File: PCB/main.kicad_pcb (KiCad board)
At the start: 2 copper layers, 112.9 x 63.7 mm, 104 parts, among them K1 HK19F-DCxxV-SHC, Q10 BC817, Q11 BC817, Q12 TPCA8120,L1Q, Q13 BC817, Q14 BC817, Q15 BC817, Q16 TPCA8120,L1Q, Q17 BC817, Q18 TPCA8120,L1Q, Q19 BC817, Q2 BC817, Q3 TPCA8120,L1Q, Q4 BC817, Q5 TPCA8120,L1Q, Q6 TPCA8120,L1Q, Q7 TPCA8120,L1Q, Q8 BC817, Q9 BC817, SW1 config, U1 ESP32-S2-DevKitM, U2 L7805

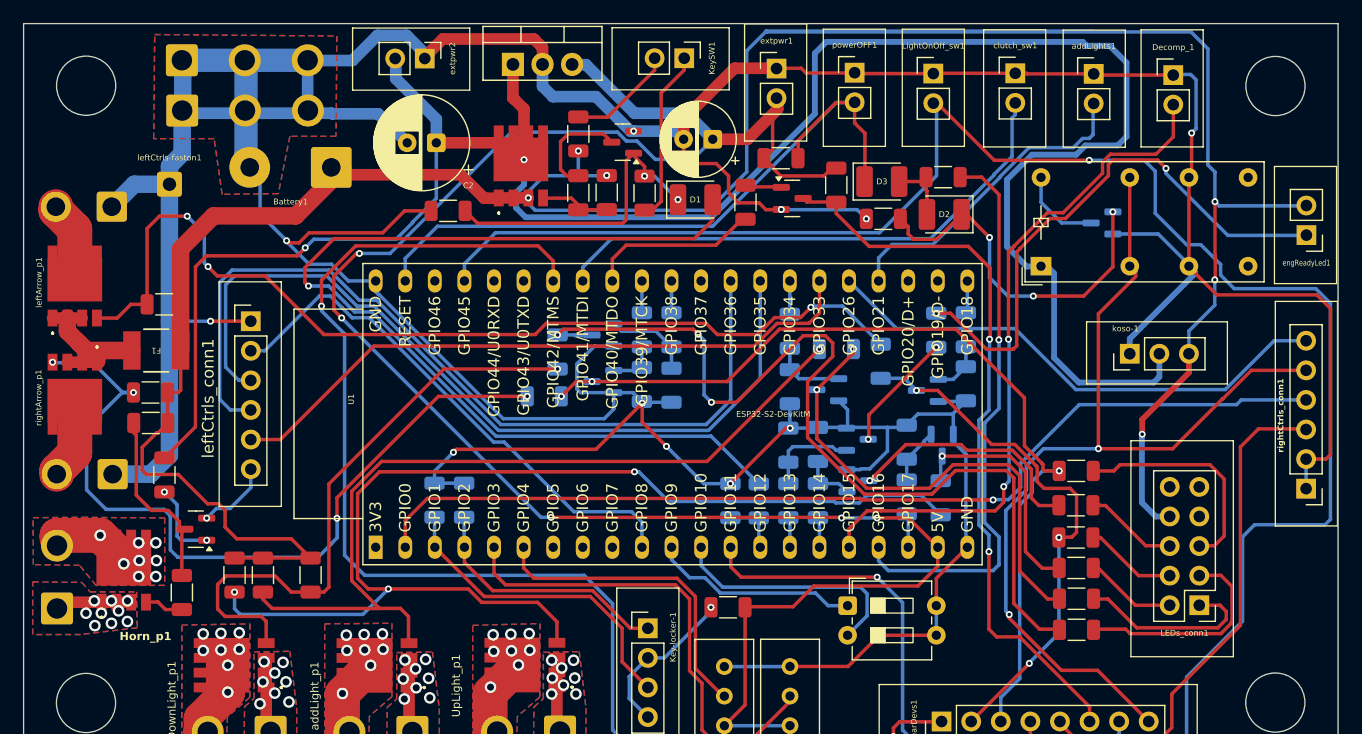
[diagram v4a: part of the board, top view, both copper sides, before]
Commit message: onnectors number reducing
Because clucth lever switch is always placed in the left side of the handle-bar, I added the pin to the left-controls connector.
The 6-pins connector has been substituted by an 8-pins one.
In this way I got two advantages:
- I have reduced the command cables in the upside of the PCB
- The left and right controls connectors are different, now
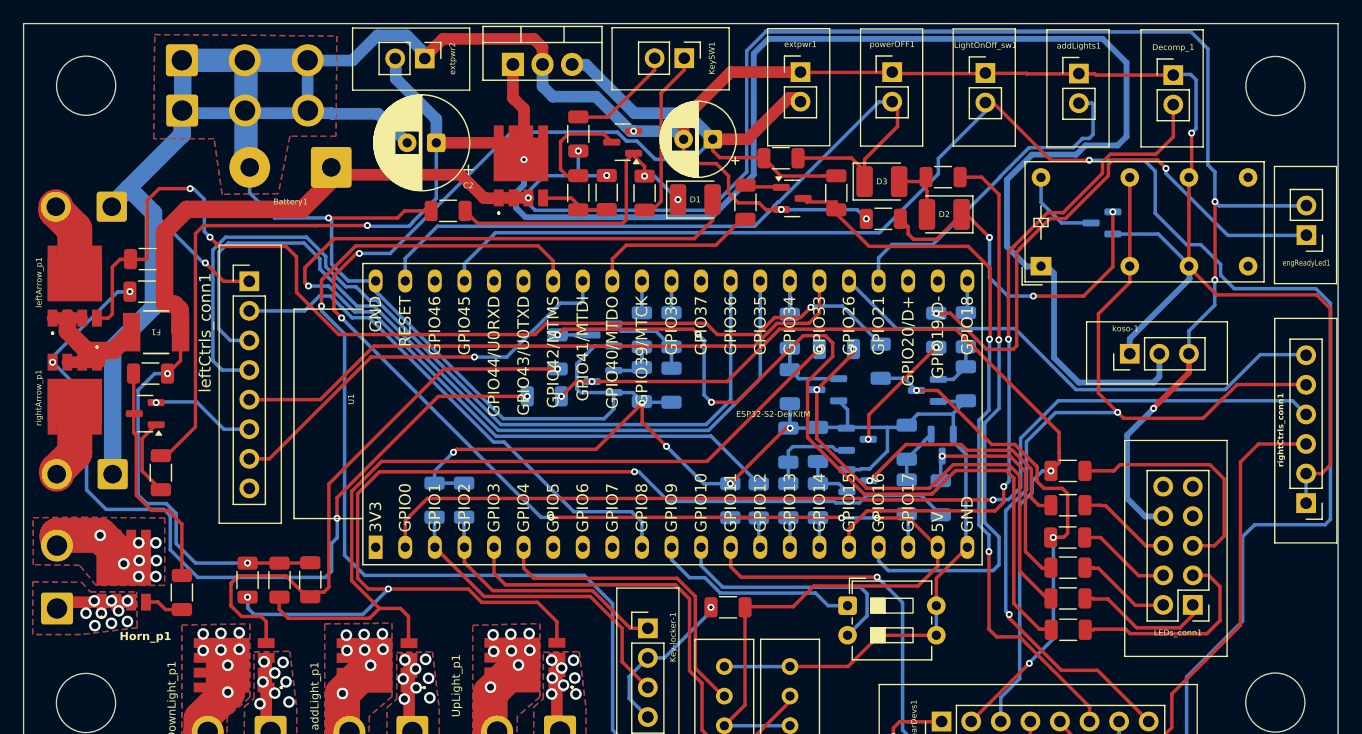
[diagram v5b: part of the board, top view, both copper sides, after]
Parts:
- removed clutch_sw1: Conn_01x02, Connector_PinHeader_2.54mm:PinHeader_1x02_P2.54mm_Vertical
- removed leftCtrls-faston1: Conn_01x01, Connector_Wire:SolderWire-0.5sqmm_1x01_D0.9mm_OD2.1mm
- leftCtrls_conn1: value Conn_01x06 -> Conn_01x08; footprint Connector_PinHeader_2.54mm:PinHeader_1x06_P2.54mm_Vertical -> Connector_PinHeader_2.54mm:PinHeader_1x08_P2.54mm_Vertical
- moved Q17 10.8 mm to (64.7, 87.2)
- moved RA13 8.67 mm to (64.8, 76.7)
- moved LightOnOff_sw1 4.47 mm to (136.8, 58.0)
- moved RA21 4.24 mm to (65.1, 83.8)
- moved RA12 4.14 mm to (64.9, 73.9)
- moved leftCtrls_conn1 3.43 mm to (73.6, 75.8)
- moved powerOFF1 3.23 mm to (128.8, 57.9)
- moved extpwr1 2.08 mm to (120.9, 57.9)
- moved F1 1.57 mm to (65.6, 80.2)
- moved RA9 1.49 mm to (76.2, 101.5)
- moved addLights1 1.27 mm to (144.8, 58.0)
- moved rightCtrls_conn1 1.24 mm to (164.3, 94.9)
- moved RA10 1.20 mm to (73.5, 101.5)
- moved RA4 0.74 mm to (143.9, 103.1)
- moved RA3 0.71 mm to (143.9, 100.4)
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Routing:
- net i_clutch: track 46.7 -> 36.1 mm, vias 0 -> 1
- net Net-(Q16-G): track 68.3 -> 74.2 mm
- net Net-(Q12-G): track 83.6 -> 89.0 mm
- net tempPower: track 187.0 -> 192.2 mm
- net i_powerOFF: track 61.0 -> 65.4 mm
- net Net-(LEDs_conn1-Pin_1): track 15.9 -> 11.6 mm
- net Net-(Q17-C): track 16.1 -> 19.9 mm
- net 5V: track 173.3 -> 176.1 mm
- net c_horn: track 6.46 -> 9.00 mm
- net c_rearLight: track 172.0 -> 169.6 mm
- net i_downLight: track 71.6 -> 73.8 mm
- net i_upLight: track 74.0 -> 76.1 mm
- net Net-(Q7-G): track 51.8 -> 49.7 mm
- net c_engineOFF: track 81.8 -> 80.1 mm
- net i_startButton: track 85.2 -> 86.9 mm
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
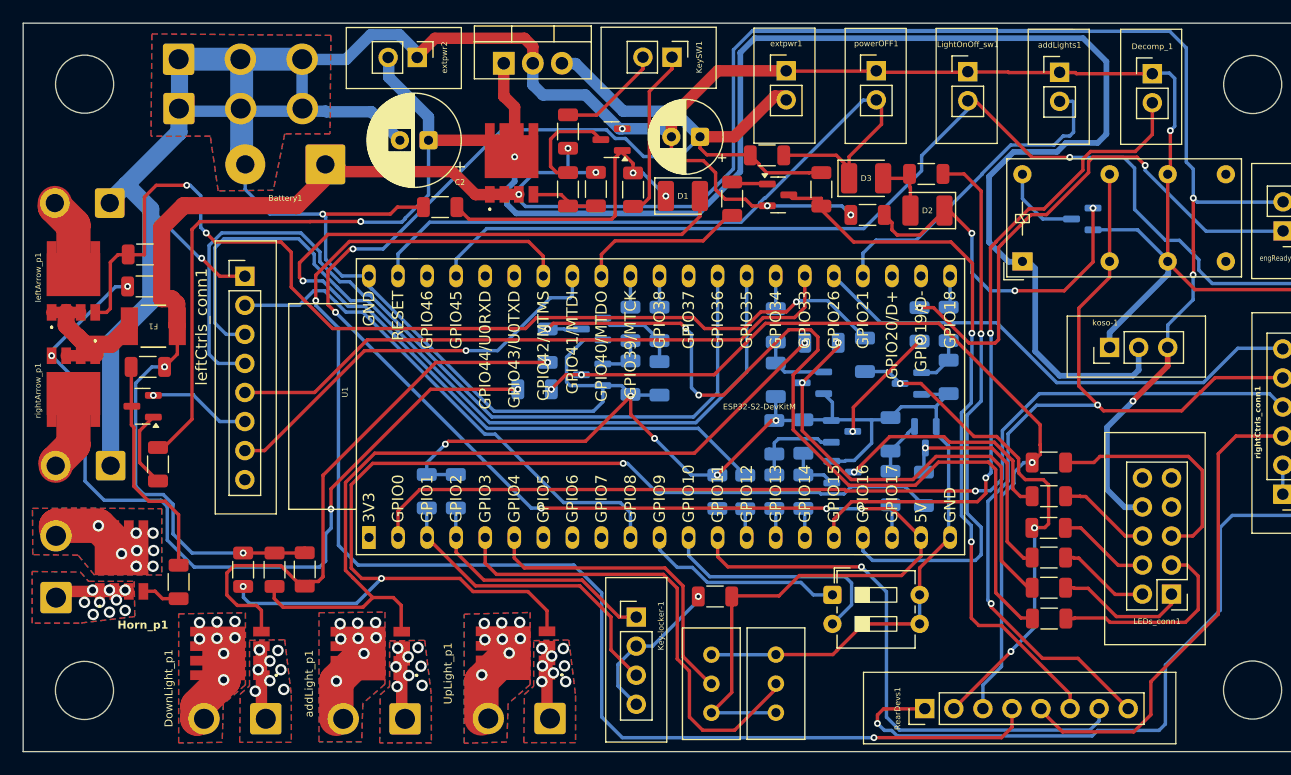
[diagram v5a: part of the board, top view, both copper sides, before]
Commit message: Less unordered cables
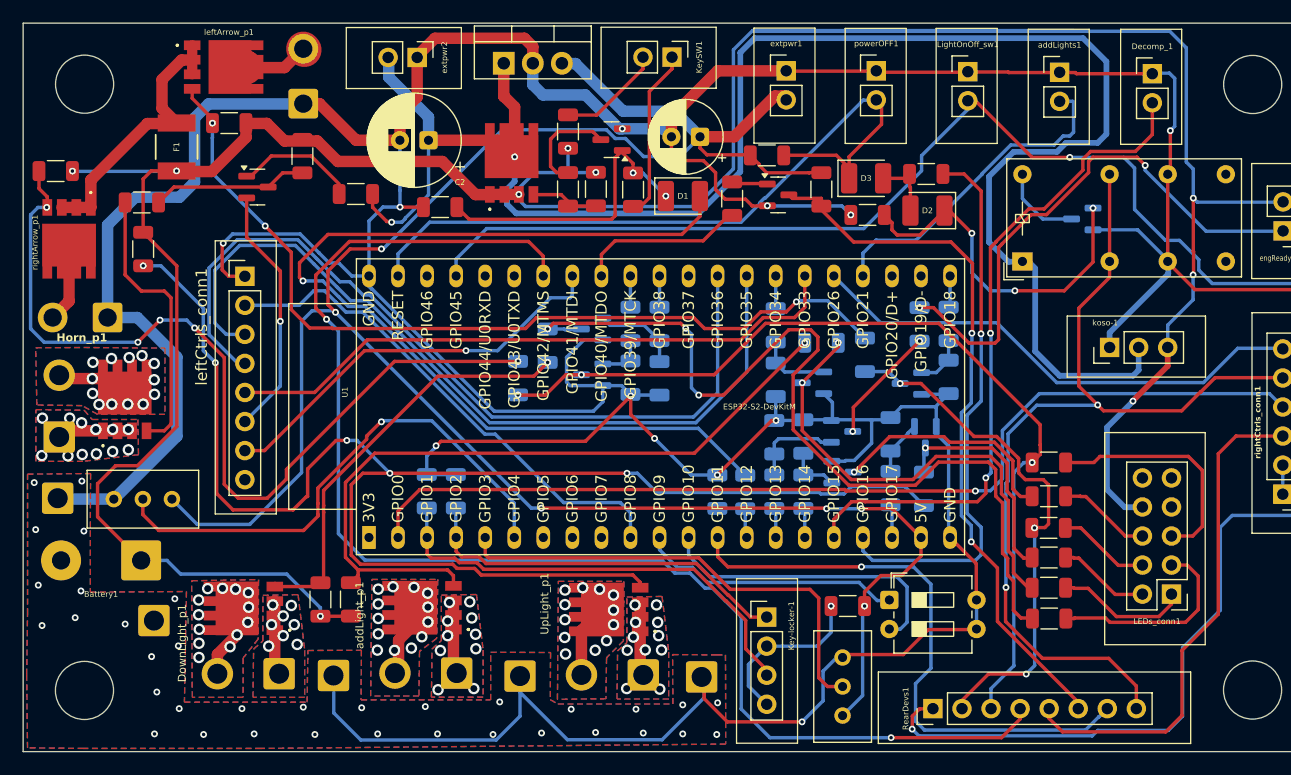
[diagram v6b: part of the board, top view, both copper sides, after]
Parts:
- removed GND-1, GND-2: ~, Connector_Wire:SolderWire-1sqmm_1x03_P5.4mm_D1.4mm_OD2.7mm
- added GND1: Conn_01x01, Connector_Wire:SolderWire-1sqmm_1x01_D1.4mm_OD2.7mm, F.Cu at (113.5, 110.9)
- added GND2: Conn_01x01, Connector_Wire:SolderWire-1sqmm_1x01_D1.4mm_OD2.7mm, F.Cu at (97.7, 110.8)
- added GND3: Conn_01x01, Connector_Wire:SolderWire-1sqmm_1x01_D1.4mm_OD2.7mm, F.Cu at (81.4, 110.7)
- added GND4: Conn_01x01, Connector_Wire:SolderWire-1sqmm_1x01_D1.4mm_OD2.7mm, F.Cu at (57.2, 95.2)
- added GND5: Conn_01x01, Connector_Wire:SolderWire-1sqmm_1x01_D1.4mm_OD2.7mm, F.Cu at (65.7, 105.9)
- moved RV2 50.7 mm to (67.2, 95.3), turned to 0 degrees
- moved Battery1 38.2 mm to (64.5, 100.7)
- moved RA26 33.3 mm to (64.6, 69.4), turned to 0 degrees
- moved RA10 29.4 mm to (64.7, 73.5)
- moved RA29 29.3 mm to (83.3, 68.7), turned to 180 degrees
- moved RA21 22.8 mm to (78.6, 65.3), turned to 90 degrees
- moved Q12 22.8 mm to (71.8, 57.6), turned to -90 degrees
- moved Q17 21.6 mm to (74.7, 68.0), turned to 0 degrees
- moved leftArrow_p1 19.0 mm to (78.7, 60.8), turned to 90 degrees
- moved F1 15.8 mm to (67.6, 64.5), turned to 90 degrees
- moved Horn_p1 14.0 mm to (57.4, 89.9)
- moved Q18 14.0 mm to (63.1, 86.6)
- moved RA12 13.6 mm to (72.2, 62.5)
- moved Q16 13.0 mm to (58.2, 72.6)
- moved rightArrow_p1 13.0 mm to (61.6, 79.5)
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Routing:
- net tempPower: track 192.2 -> 156.9 mm
- net Net-(Q6-G): track 94.8 -> 129.4 mm, vias 3 -> 5
- net GND: track 458.5 -> 486.6 mm, vias 11 -> 47
- net +12V: track 245.8 -> 272.6 mm, vias 8 -> 9
- net Net-(Q18-G): track 3.36 -> 24.6 mm
- net Net-(U1-GPIO4/TOUCH4/ADC1_CH3): track 27.2 -> 46.0 mm, vias 0 -> 1
- net c_horn: track 9.00 -> 22.0 mm
- net 5V: track 176.1 -> 189.1 mm, vias 5 -> 6
- net Net-(Q7-G): track 49.7 -> 36.8 mm
- net i_Vx1: track 27.5 -> 39.8 mm
- net Net-(Q12-G): track 89.0 -> 76.9 mm
- net i_Vx2: track 22.0 -> 33.3 mm
- net Net-(Q12-S_1): track 15.4 -> 24.7 mm
- net Net-(Q5-G): track 71.7 -> 64.2 mm
- net Net-(Q17-C): track 19.9 -> 13.6 mm
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
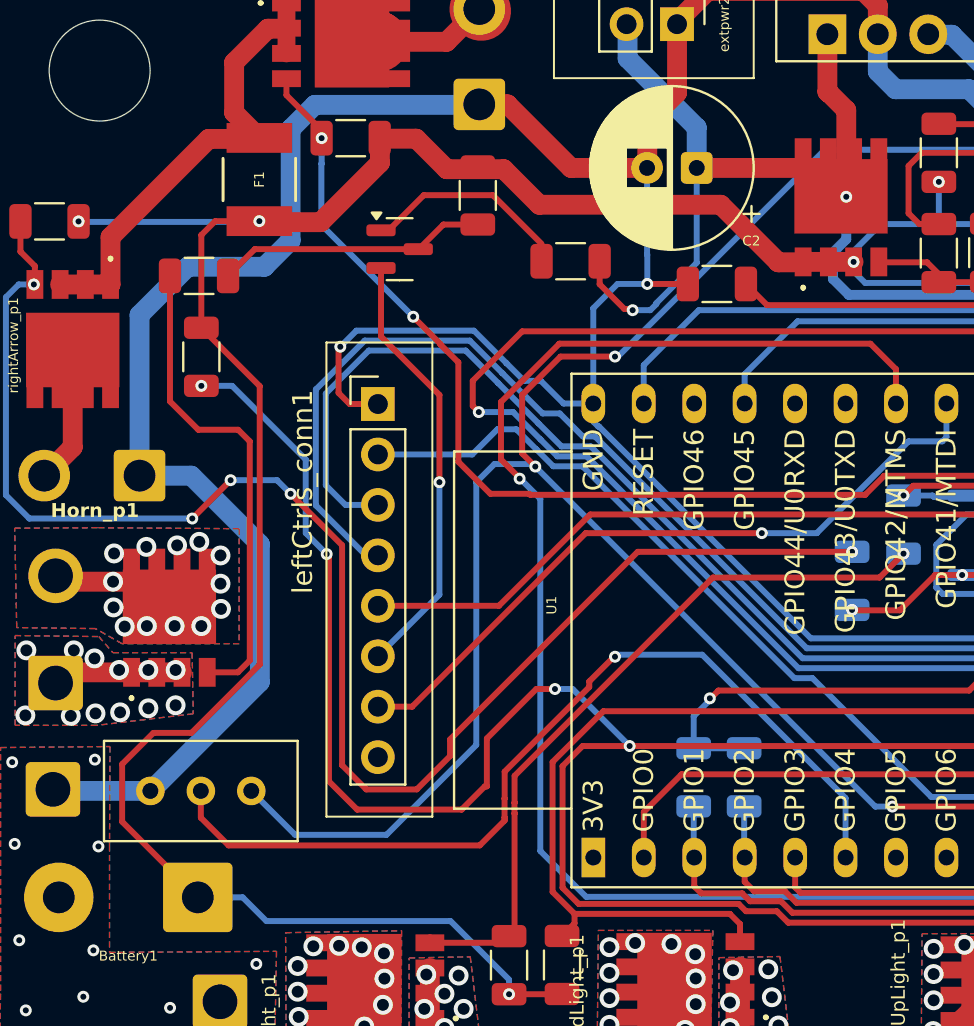
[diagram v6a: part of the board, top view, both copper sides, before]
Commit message: Wrong electric track size fixed
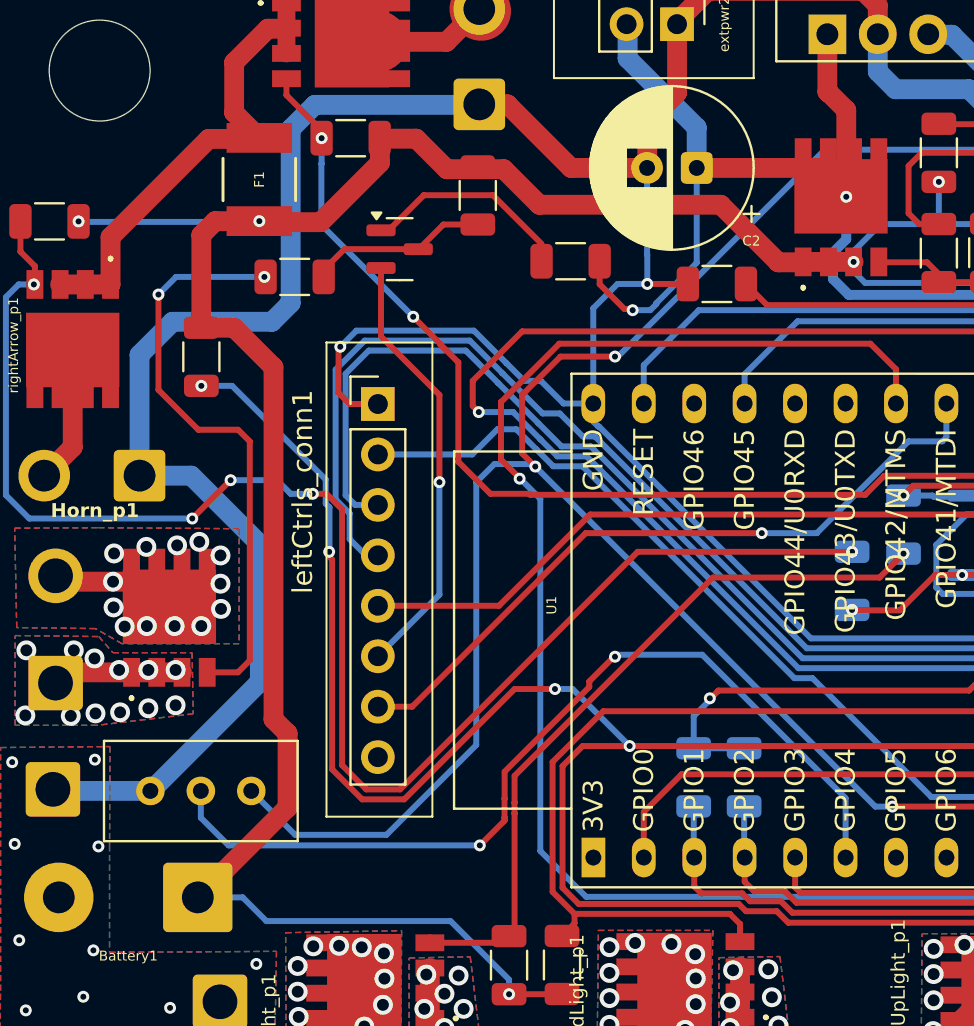
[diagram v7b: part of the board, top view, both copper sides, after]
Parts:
- moved RA26 4.82 mm to (69.4, 69.4)
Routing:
- net Net-(Q18-G): track 24.6 -> 29.6 mm, vias 0 -> 2
- net Net-(Q17-C): track 13.6 -> 9.06 mm
- net Net-(Q6-G): track 129.4 -> 127.1 mm
- net +12V: track 272.6 -> 270.5 mm
- net i_downLight: track 71.7 -> 70.6 mm
- net i_upLight: track 73.0 -> 72.2 mm
- net GND: track 486.6 -> 487.3 mm
- net Net-(Q16-G): track 77.4 -> 78.0 mm
- net Net-(U1-GPIO4/TOUCH4/ADC1_CH3): vias 1 -> 2
